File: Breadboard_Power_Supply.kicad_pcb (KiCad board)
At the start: 2 copper layers, 46.3 x 24.3 mm, 14 parts, among them J3 Conn_01x03_Pin, J5 Screw_Terminal_01x02, J6 Barrel_Jack_Switch, U1 LM7805_TO220, U2 LM317_TO-220

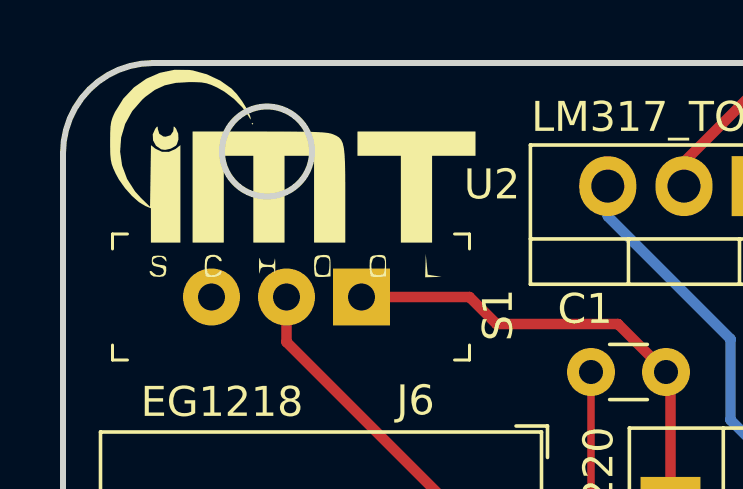
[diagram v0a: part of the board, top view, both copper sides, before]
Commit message: Updated the Logo
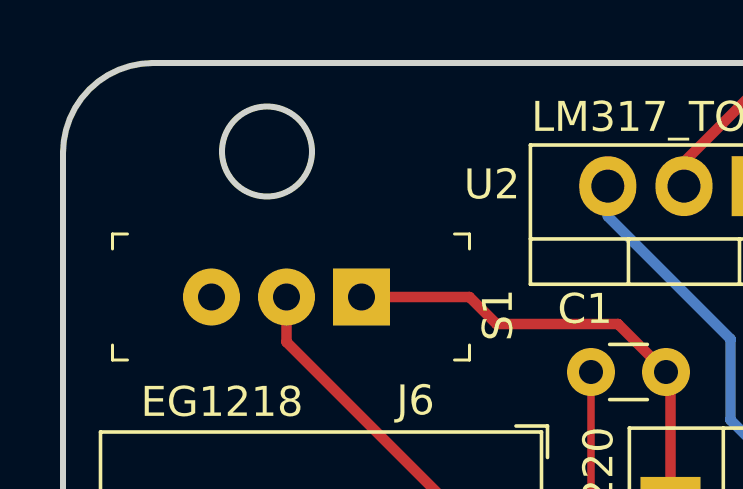
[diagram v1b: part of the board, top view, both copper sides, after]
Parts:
- removed the G*** at (43.0, 40.1)
- added G***: LOGO, logo_Footprints:imt_new3, B.Cu at (39.4, 52.9)
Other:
- board text removed: "Designed by"
- board text removed: "IMT SCHOOL"
